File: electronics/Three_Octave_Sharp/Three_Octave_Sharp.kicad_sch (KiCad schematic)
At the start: 33 parts, among them J1 FFC Connector, J1 HRO_TYPE-C-31-M-12, SW21 Alps_Alpine_SKRP, SW22 Alps_Alpine_SKRP, U1 AP2112K-3.3, U2 Raspberry_Pi_RP2040, U2 W25Q64JVXGIQ, Y1 12MHz

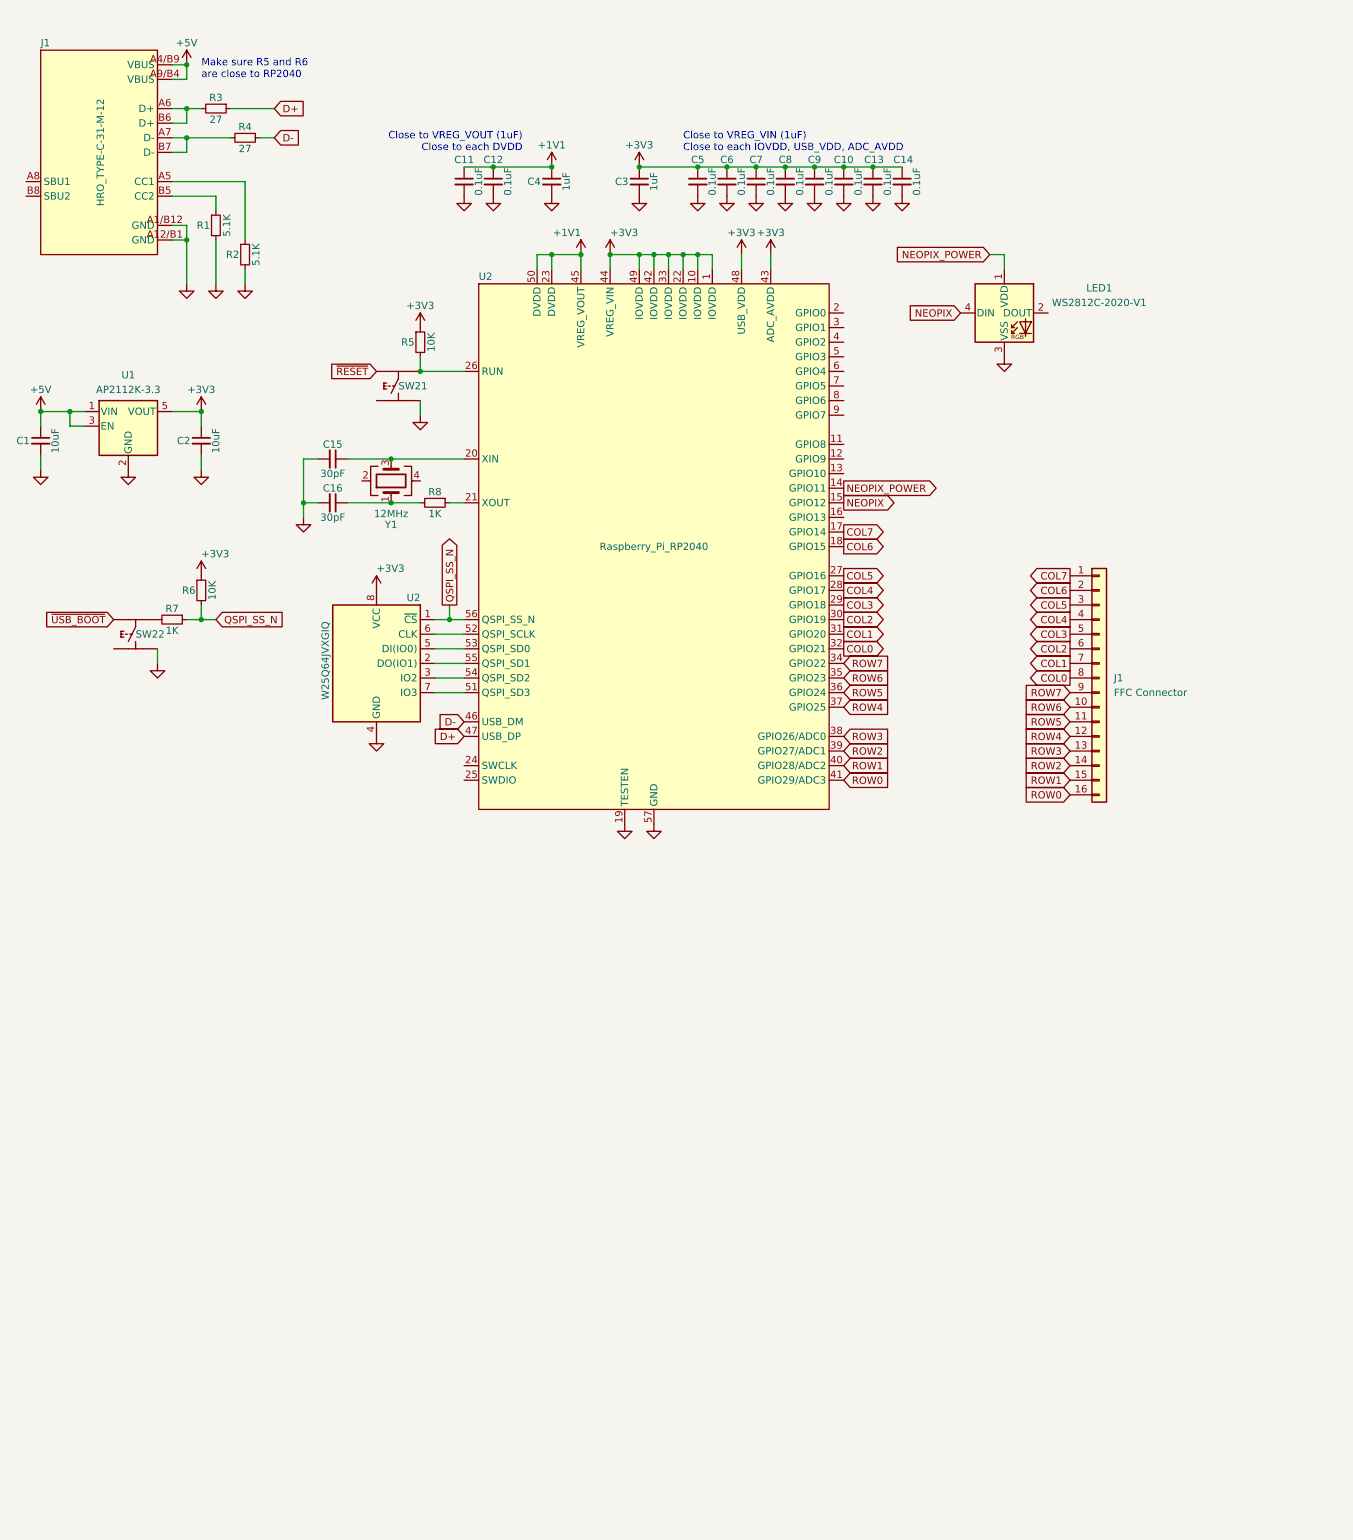
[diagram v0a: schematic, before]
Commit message: Add schematic and PCB design copied from Five Octave
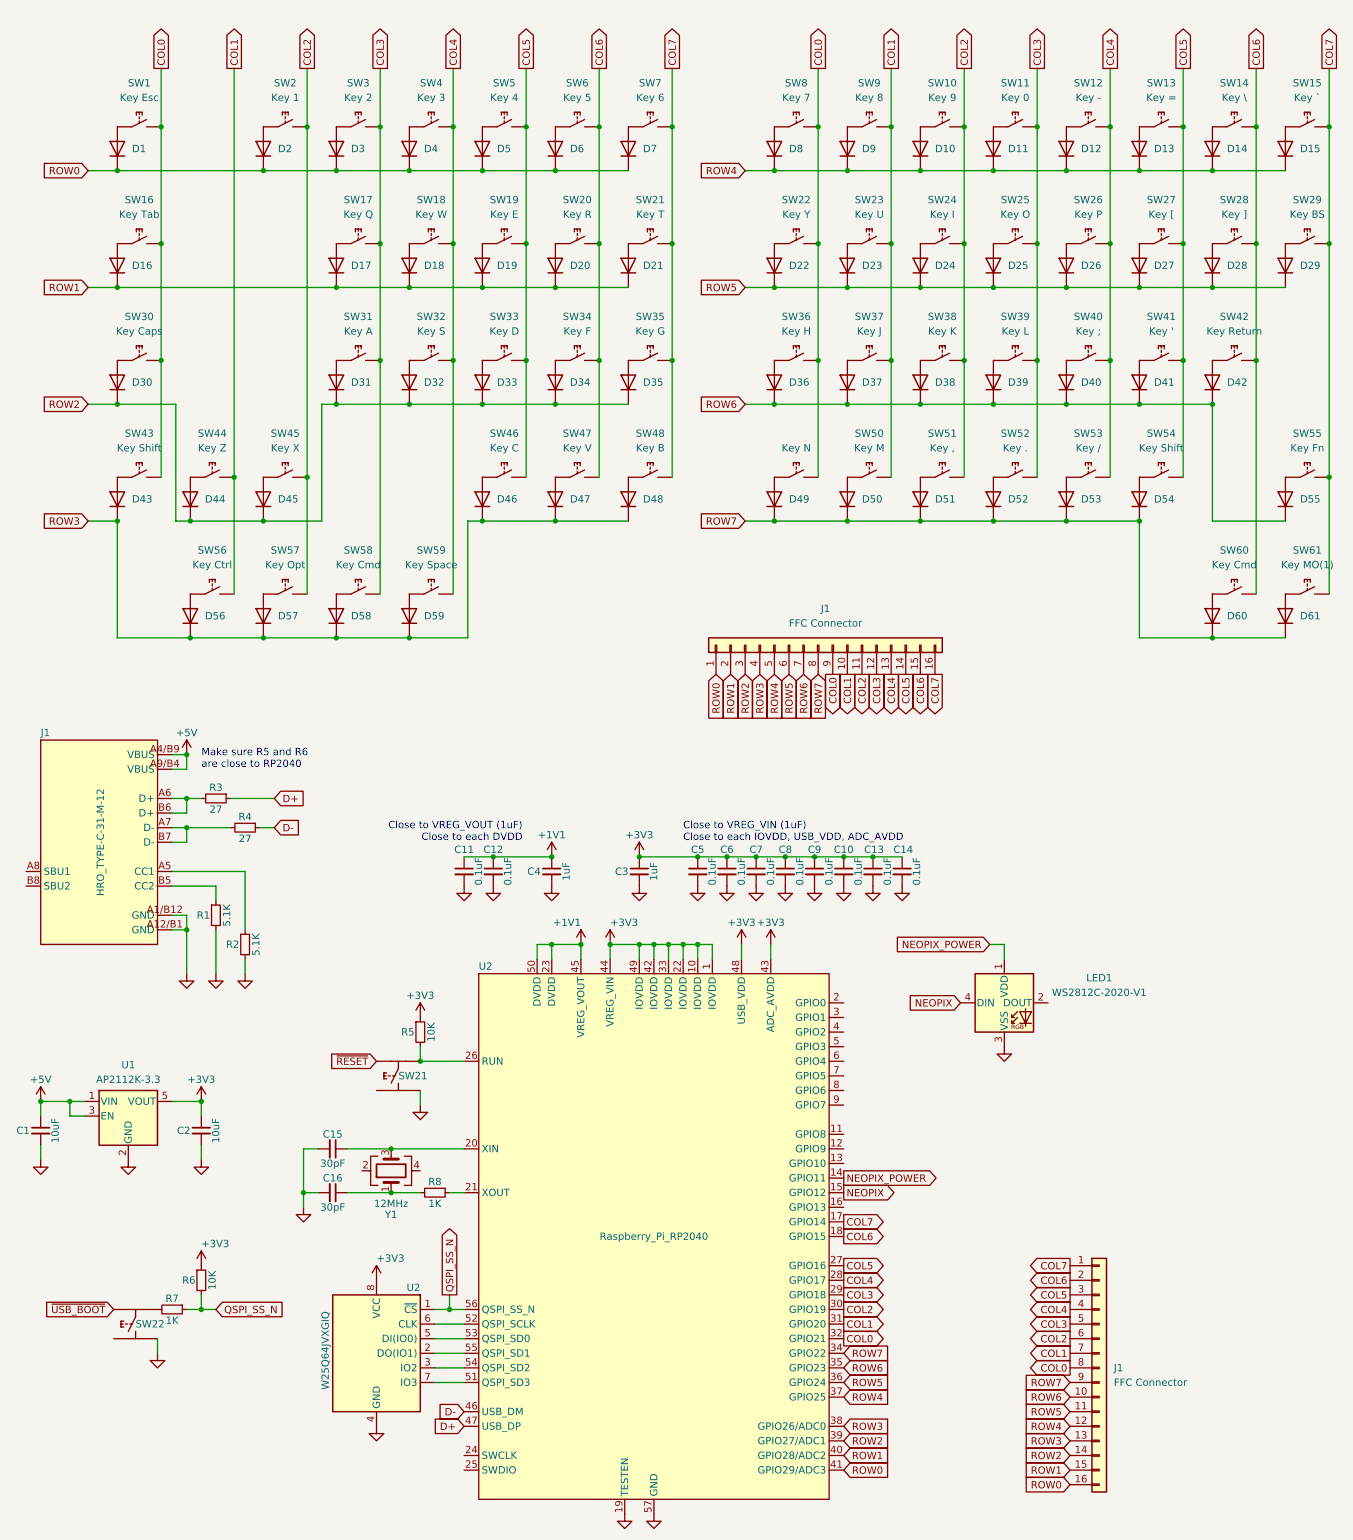
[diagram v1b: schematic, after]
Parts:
- added D1, D10, D11, D12, D13, D14, D15, D16, D17, D18, D19, D2, D20, D21, D22, D23, D24, D25, D26, D27, D28, D29, D3, D30, D31, D32, D33, D34, D35, D36, D37, D38, D39, D4, D40, D41, D42, D43, D44, D45, D46, D47, D48, D49, D5, D50, D51, D52, D53, D54, D55, D56, D57, D58, D59, D6, D60, D61, D7, D8, D9: 1N4148WS, Project_Library:D_SOD-323F, symbol Diode:1N4148WS
- added J1: FFC Connector, Project_Library:JUSHUO_AFC01-S16FCC-00, symbol Connector_Generic:Conn_01x16
- added SW1: Key Esc, Project_Library:Hot_Swap_Socket_CPG151101S11, symbol Project_Library:SW_Hot_Swap_Socket
- added SW10: Key 9, Project_Library:Hot_Swap_Socket_CPG151101S11, symbol Project_Library:SW_Hot_Swap_Socket
- added SW11: Key 0, Project_Library:Hot_Swap_Socket_CPG151101S11, symbol Project_Library:SW_Hot_Swap_Socket
- added SW12: Key -, Project_Library:Hot_Swap_Socket_CPG151101S11, symbol Project_Library:SW_Hot_Swap_Socket
- added SW13: Key =, Project_Library:Hot_Swap_Socket_CPG151101S11, symbol Project_Library:SW_Hot_Swap_Socket
- added SW14: Key \, Project_Library:Hot_Swap_Socket_CPG151101S11, symbol Project_Library:SW_Hot_Swap_Socket
- added SW15: Key `, Project_Library:Hot_Swap_Socket_CPG151101S11, symbol Project_Library:SW_Hot_Swap_Socket
- added SW16: Key Tab, Project_Library:Hot_Swap_Socket_CPG151101S11, symbol Project_Library:SW_Hot_Swap_Socket
- added SW17: Key Q, Project_Library:Hot_Swap_Socket_CPG151101S11, symbol Project_Library:SW_Hot_Swap_Socket
- added SW18: Key W, Project_Library:Hot_Swap_Socket_CPG151101S11, symbol Project_Library:SW_Hot_Swap_Socket
- added SW19: Key E, Project_Library:Hot_Swap_Socket_CPG151101S11, symbol Project_Library:SW_Hot_Swap_Socket
- added SW2: Key 1, Project_Library:Hot_Swap_Socket_CPG151101S11, symbol Project_Library:SW_Hot_Swap_Socket
- added SW20: Key R, Project_Library:Hot_Swap_Socket_CPG151101S11, symbol Project_Library:SW_Hot_Swap_Socket
- added SW21: Key T, Project_Library:Hot_Swap_Socket_CPG151101S11, symbol Project_Library:SW_Hot_Swap_Socket
- added SW22: Key Y, Project_Library:Hot_Swap_Socket_CPG151101S11, symbol Project_Library:SW_Hot_Swap_Socket
- added SW23: Key U, Project_Library:Hot_Swap_Socket_CPG151101S11, symbol Project_Library:SW_Hot_Swap_Socket
- added SW24: Key I, Project_Library:Hot_Swap_Socket_CPG151101S11, symbol Project_Library:SW_Hot_Swap_Socket
- added SW25: Key O, Project_Library:Hot_Swap_Socket_CPG151101S11, symbol Project_Library:SW_Hot_Swap_Socket
- added SW26: Key P, Project_Library:Hot_Swap_Socket_CPG151101S11, symbol Project_Library:SW_Hot_Swap_Socket
- added SW27: Key [, Project_Library:Hot_Swap_Socket_CPG151101S11, symbol Project_Library:SW_Hot_Swap_Socket
- added SW28: Key ], Project_Library:Hot_Swap_Socket_CPG151101S11, symbol Project_Library:SW_Hot_Swap_Socket
- added SW29: Key BS, Project_Library:Hot_Swap_Socket_CPG151101S11, symbol Project_Library:SW_Hot_Swap_Socket
- added SW3: Key 2, Project_Library:Hot_Swap_Socket_CPG151101S11, symbol Project_Library:SW_Hot_Swap_Socket
- added SW30: Key Caps, Project_Library:Hot_Swap_Socket_CPG151101S11, symbol Project_Library:SW_Hot_Swap_Socket
- added SW31: Key A, Project_Library:Hot_Swap_Socket_CPG151101S11, symbol Project_Library:SW_Hot_Swap_Socket
- added SW32: Key S, Project_Library:Hot_Swap_Socket_CPG151101S11, symbol Project_Library:SW_Hot_Swap_Socket
- added SW33: Key D, Project_Library:Hot_Swap_Socket_CPG151101S11, symbol Project_Library:SW_Hot_Swap_Socket
- added SW34: Key F, Project_Library:Hot_Swap_Socket_CPG151101S11, symbol Project_Library:SW_Hot_Swap_Socket
- added SW35: Key G, Project_Library:Hot_Swap_Socket_CPG151101S11, symbol Project_Library:SW_Hot_Swap_Socket
- added SW36: Key H, Project_Library:Hot_Swap_Socket_CPG151101S11, symbol Project_Library:SW_Hot_Swap_Socket
- added SW37: Key J, Project_Library:Hot_Swap_Socket_CPG151101S11, symbol Project_Library:SW_Hot_Swap_Socket
- added SW38: Key K, Project_Library:Hot_Swap_Socket_CPG151101S11, symbol Project_Library:SW_Hot_Swap_Socket
- added SW39: Key L, Project_Library:Hot_Swap_Socket_CPG151101S11, symbol Project_Library:SW_Hot_Swap_Socket
- added SW4: Key 3, Project_Library:Hot_Swap_Socket_CPG151101S11, symbol Project_Library:SW_Hot_Swap_Socket
- added SW40: Key ;, Project_Library:Hot_Swap_Socket_CPG151101S11, symbol Project_Library:SW_Hot_Swap_Socket
- added SW41: Key ', Project_Library:Hot_Swap_Socket_CPG151101S11, symbol Project_Library:SW_Hot_Swap_Socket
- added SW42: Key Return, Project_Library:Hot_Swap_Socket_CPG151101S11, symbol Project_Library:SW_Hot_Swap_Socket
- added SW43, SW54: Key Shift, Project_Library:Hot_Swap_Socket_CPG151101S11, symbol Project_Library:SW_Hot_Swap_Socket
- added SW44: Key Z, Project_Library:Hot_Swap_Socket_CPG151101S11, symbol Project_Library:SW_Hot_Swap_Socket
- added SW45: Key X, Project_Library:Hot_Swap_Socket_CPG151101S11, symbol Project_Library:SW_Hot_Swap_Socket
- added SW46: Key C, Project_Library:Hot_Swap_Socket_CPG151101S11, symbol Project_Library:SW_Hot_Swap_Socket
- added SW47: Key V, Project_Library:Hot_Swap_Socket_CPG151101S11, symbol Project_Library:SW_Hot_Swap_Socket
- added SW48: Key B, Project_Library:Hot_Swap_Socket_CPG151101S11, symbol Project_Library:SW_Hot_Swap_Socket
- added SW49: Key N, Project_Library:Hot_Swap_Socket_CPG151101S11, symbol Project_Library:SW_Hot_Swap_Socket
- added SW5: Key 4, Project_Library:Hot_Swap_Socket_CPG151101S11, symbol Project_Library:SW_Hot_Swap_Socket
- added SW50: Key M, Project_Library:Hot_Swap_Socket_CPG151101S11, symbol Project_Library:SW_Hot_Swap_Socket
- added SW51: Key ,, Project_Library:Hot_Swap_Socket_CPG151101S11, symbol Project_Library:SW_Hot_Swap_Socket
- added SW52: Key ., Project_Library:Hot_Swap_Socket_CPG151101S11, symbol Project_Library:SW_Hot_Swap_Socket
- added SW53: Key /, Project_Library:Hot_Swap_Socket_CPG151101S11, symbol Project_Library:SW_Hot_Swap_Socket
- added SW55: Key Fn, Project_Library:Hot_Swap_Socket_CPG151101S11, symbol Project_Library:SW_Hot_Swap_Socket
- added SW56: Key Ctrl, Project_Library:Hot_Swap_Socket_CPG151101S11, symbol Project_Library:SW_Hot_Swap_Socket
- added SW57: Key Opt, Project_Library:Hot_Swap_Socket_CPG151101S11, symbol Project_Library:SW_Hot_Swap_Socket
- added SW58, SW60: Key Cmd, Project_Library:Hot_Swap_Socket_CPG151101S11, symbol Project_Library:SW_Hot_Swap_Socket
- added SW59: Key Space, Project_Library:Hot_Swap_Socket_CPG151101S11, symbol Project_Library:SW_Hot_Swap_Socket
- added SW6: Key 5, Project_Library:Hot_Swap_Socket_CPG151101S11, symbol Project_Library:SW_Hot_Swap_Socket
- added SW61: Key MO(1), Project_Library:Hot_Swap_Socket_CPG151101S11, symbol Project_Library:SW_Hot_Swap_Socket
- added SW7: Key 6, Project_Library:Hot_Swap_Socket_CPG151101S11, symbol Project_Library:SW_Hot_Swap_Socket
- added SW8: Key 7, Project_Library:Hot_Swap_Socket_CPG151101S11, symbol Project_Library:SW_Hot_Swap_Socket
- added SW9: Key 8, Project_Library:Hot_Swap_Socket_CPG151101S11, symbol Project_Library:SW_Hot_Swap_Socket
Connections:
- net COL0: now also J1.9 (Pin_9), SW1.2, SW16.2, SW22.2, SW30.2, SW36.2, SW43.2, SW49.2, SW8.2
- net COL1: now also J1.10 (Pin_10), SW23.2, SW37.2, SW44.2, SW50.2, SW56.2, SW9.2
- net COL2: now also J1.11 (Pin_11), SW10.2, SW2.2, SW24.2, SW38.2, SW45.2, SW51.2, SW57.2
- net COL3: now also J1.12 (Pin_12), SW11.2, SW17.2, SW25.2, SW3.2, SW31.2, SW39.2, SW52.2, SW58.2
- net COL4: now also J1.13 (Pin_13), SW12.2, SW18.2, SW26.2, SW32.2, SW4.2, SW40.2, SW53.2, SW59.2
- net COL5: now also J1.14 (Pin_14), SW13.2, SW19.2, SW27.2, SW33.2, SW41.2, SW46.2, SW5.2, SW54.2
- net COL6: now also J1.15 (Pin_15), SW14.2, SW20.2, SW28.2, SW34.2, SW42.2, SW47.2, SW6.2, SW60.2
- net COL7: now also J1.16 (Pin_16), SW15.2, SW21.2, SW29.2, SW35.2, SW48.2, SW55.2, SW61.2, SW7.2
- net ROW0: now also D1.1 (K), D2.1 (K), D3.1 (K), D4.1 (K), D5.1 (K), D6.1 (K), D7.1 (K), J1.1 (Pin_1)
- net ROW1: now also D16.1 (K), D17.1 (K), D18.1 (K), D19.1 (K), D20.1 (K), D21.1 (K), J1.2 (Pin_2)
- net ROW2: now also D30.1 (K), D31.1 (K), D32.1 (K), D33.1 (K), D34.1 (K), D35.1 (K), D44.1 (K), D45.1 (K), J1.3 (Pin_3)
- net ROW3: now also D43.1 (K), D46.1 (K), D47.1 (K), D48.1 (K), D56.1 (K), D57.1 (K), D58.1 (K), D59.1 (K), J1.4 (Pin_4)
- net ROW4: now also D10.1 (K), D11.1 (K), D12.1 (K), D13.1 (K), D14.1 (K), D15.1 (K), D8.1 (K), D9.1 (K), J1.5 (Pin_5)
- net ROW5: now also D22.1 (K), D23.1 (K), D24.1 (K), D25.1 (K), D26.1 (K), D27.1 (K), D28.1 (K), D29.1 (K), J1.6 (Pin_6)
- net ROW6: now also D36.1 (K), D37.1 (K), D38.1 (K), D39.1 (K), D40.1 (K), D41.1 (K), D42.1 (K), D55.1 (K), J1.7 (Pin_7)
- net ROW7: now also D49.1 (K), D50.1 (K), D51.1 (K), D52.1 (K), D53.1 (K), D54.1 (K), D60.1 (K), D61.1 (K), J1.8 (Pin_8)
- new net: D45.2 (A), SW45.1
- new net: D4.2 (A), SW4.1
- new net: D53.2 (A), SW53.1
- new net: D56.2 (A), SW56.1
- new net: D37.2 (A), SW37.1
- new net: D5.2 (A), SW5.1
- new net: D35.2 (A), SW35.1
- new net: D40.2 (A), SW40.1
- new net: D59.2 (A), SW59.1
- new net: D42.2 (A), SW42.1
- new net: D16.2 (A), SW16.1
- new net: D1.2 (A), SW1.1
- new net: D15.2 (A), SW15.1
- new net: D50.2 (A), SW50.1
- new net: D13.2 (A), SW13.1
- new net: D19.2 (A), SW19.1
- new net: D33.2 (A), SW33.1
- new net: D9.2 (A), SW9.1
- new net: D12.2 (A), SW12.1
- new net: D41.2 (A), SW41.1
- new net: D27.2 (A), SW27.1
- new net: D10.2 (A), SW10.1
- new net: D2.2 (A), SW2.1
- new net: D23.2 (A), SW23.1
- new net: D49.2 (A), SW49.1
- new net: D14.2 (A), SW14.1
- new net: D8.2 (A), SW8.1
- new net: D47.2 (A), SW47.1
- new net: D7.2 (A), SW7.1
- new net: D21.2 (A), SW21.1
- new net: D20.2 (A), SW20.1
- new net: D39.2 (A), SW39.1
- new net: D38.2 (A), SW38.1
- new net: D6.2 (A), SW6.1
- new net: D46.2 (A), SW46.1
- new net: D29.2 (A), SW29.1
- new net: D28.2 (A), SW28.1
- new net: D25.2 (A), SW25.1
- new net: D18.2 (A), SW18.1
- new net: D32.2 (A), SW32.1
- new net: D61.2 (A), SW61.1
- new net: D52.2 (A), SW52.1
- new net: D60.2 (A), SW60.1
- new net: D57.2 (A), SW57.1
- new net: D30.2 (A), SW30.1
- new net: D26.2 (A), SW26.1
- new net: D34.2 (A), SW34.1
- new net: D22.2 (A), SW22.1
- new net: D17.2 (A), SW17.1
- new net: D43.2 (A), SW43.1
- new net: D54.2 (A), SW54.1
- new net: D55.2 (A), SW55.1
- new net: D36.2 (A), SW36.1
- new net: D3.2 (A), SW3.1
- new net: D11.2 (A), SW11.1
- new net: D24.2 (A), SW24.1
- new net: D31.2 (A), SW31.1
- new net: D44.2 (A), SW44.1
- new net: D48.2 (A), SW48.1
- new net: D51.2 (A), SW51.1
- new net: D58.2 (A), SW58.1
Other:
- moved on the sheet: C1, C10, C11, C12, C13, C14, C15, C16, C2, C3, C4, C5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
